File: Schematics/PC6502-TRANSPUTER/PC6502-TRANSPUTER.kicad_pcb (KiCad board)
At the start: 4 copper layers, 100 x 100 mm, 52 parts, among them J1 BUS, J2 Conn_01x03, J3 Conn_01x03, J4 Conn_02x08_Odd_Even, J5 Conn_02x05_Odd_Even, J6 Conn_01x03, J7 Conn_01x03, U1 SN74LVC1G125DBV, U11 IMSC011, U2 ATF1502AS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

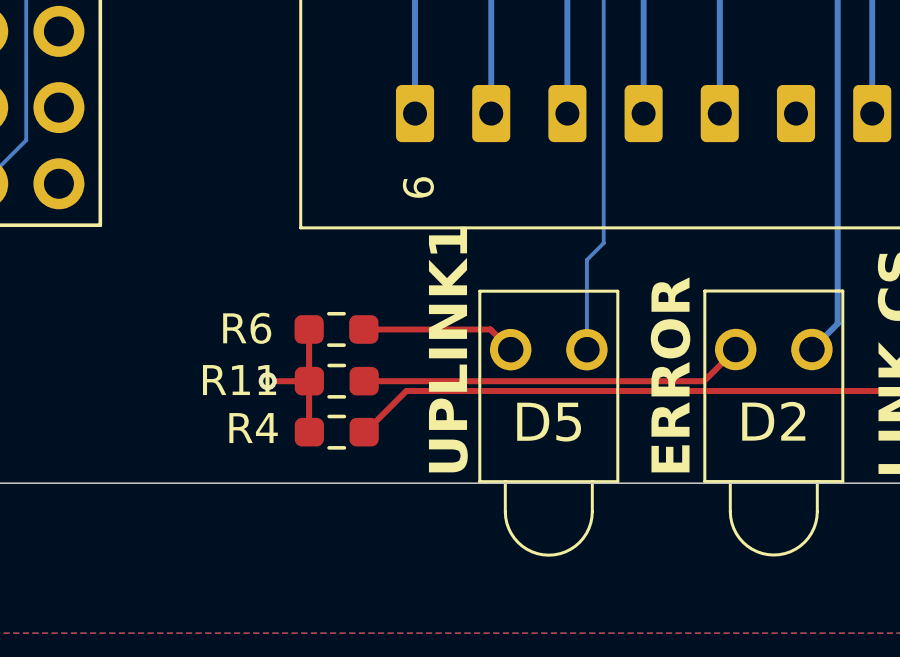
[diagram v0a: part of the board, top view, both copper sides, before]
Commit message: Updated Transputer CPLD and Basic code
writing and reading to/from the TRAM now works!
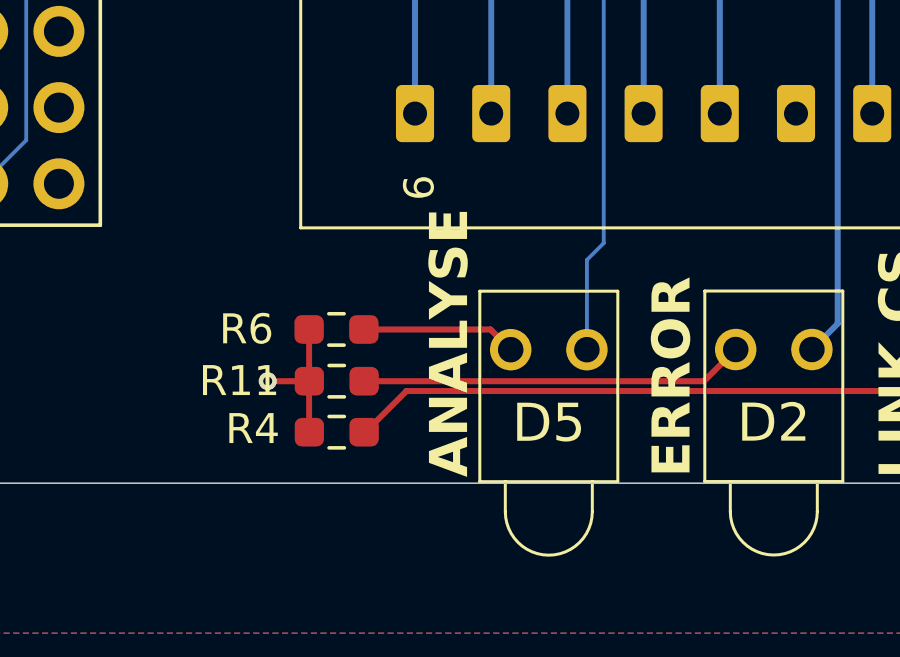
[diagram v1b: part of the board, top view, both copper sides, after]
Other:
- board text added: "ANALYSE"
- board text removed: "UPLINK1"
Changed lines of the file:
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@@
 			(psa4output no)
 			(plot_black_and_white yes)
+			(plotinvisibletext no)
 			(sketchpadsonfab no)
 			(plotpadnumbers no)
@@
 		)
 	)
-	(gr_text "UPLINK1"
+	(gr_text "ANALYSE"
 		(at 165.7 144.8 90)
 		(layer "F.SilkS")
